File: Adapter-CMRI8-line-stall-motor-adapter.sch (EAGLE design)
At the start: 4 parts

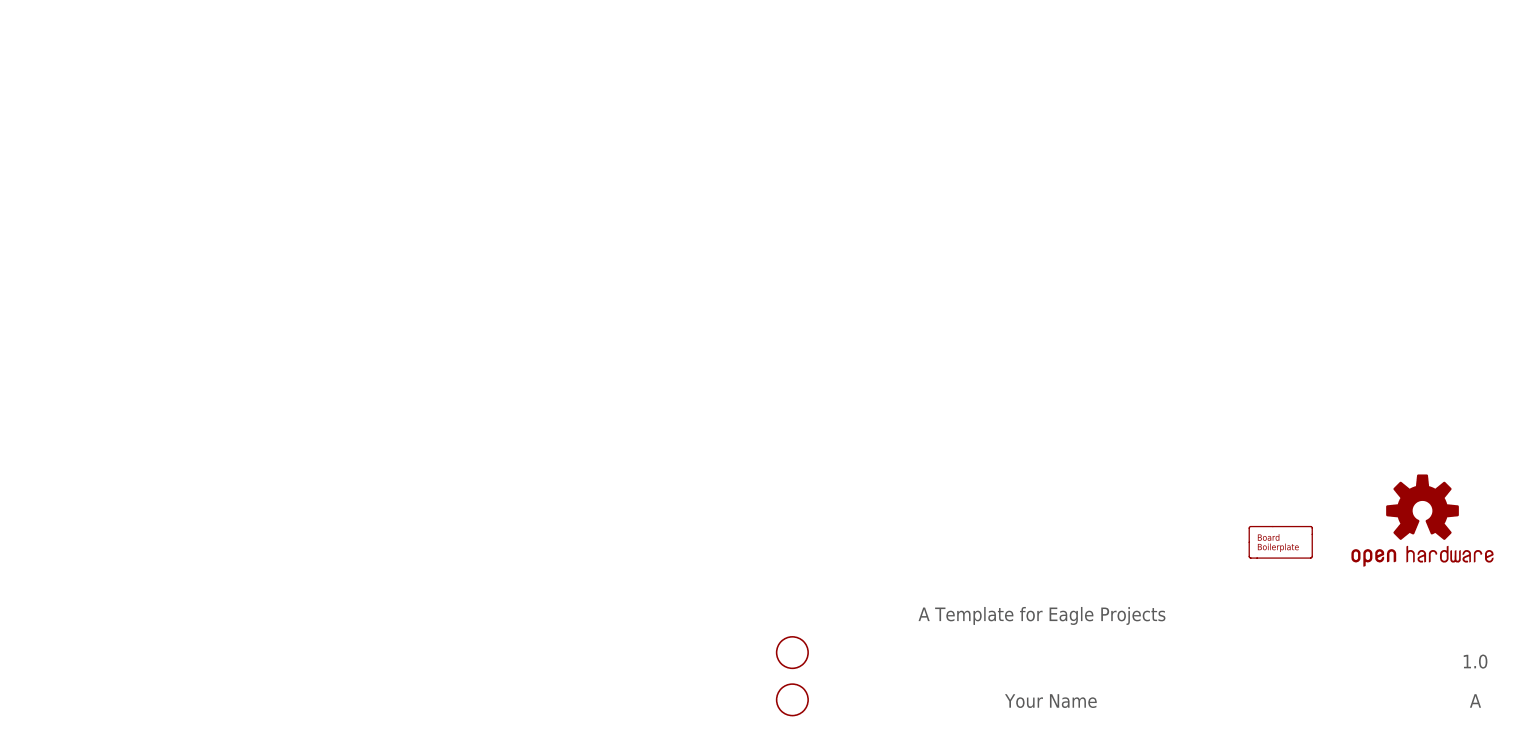
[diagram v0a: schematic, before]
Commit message: added the CMRI-35mm board as a start
modifying the CMRI-3.5 mm board
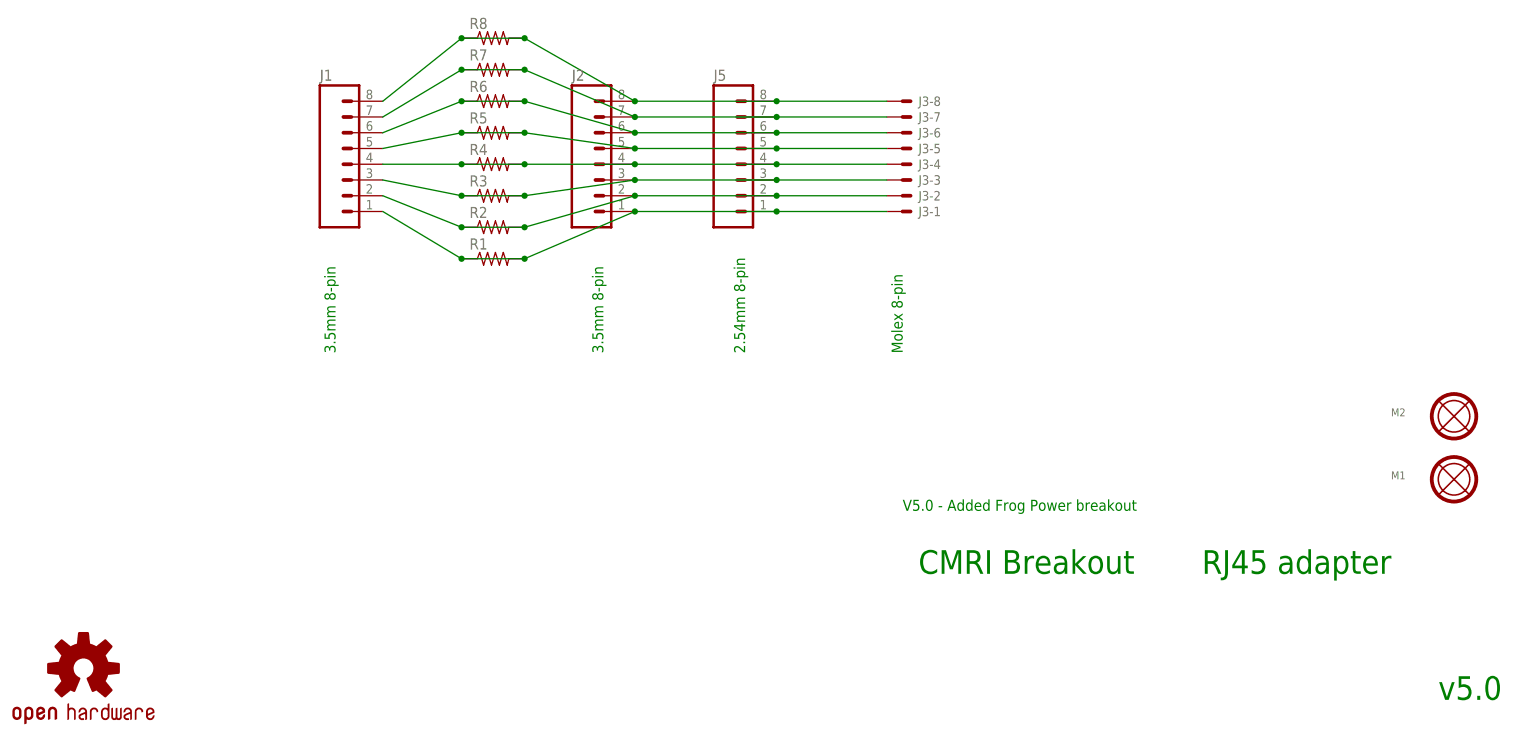
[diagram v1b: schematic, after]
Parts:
- removed BOARD1: BOARD80X100, SPCoast:BOARD80X100
- removed FID1, FID2: FIDUCIAL, SPCoast:FIDUCIAL
- removed OSHW1: DOC-OSHW-LOGO-M, SPCoast:DOC-OSHW-LOGO-M
- added J1, J2: (no value), SPCoast:CONNECTOR-M083.5MM-8
- added J3: (no value), SPCoast:KK-156-8F
- added J5: (no value), SPCoast:CONNECTOR-M08LOCK
- added M1, M2: MOUNTINGHOLE, SPCoast:MOUNTINGHOLE
- added R1, R2, R3, R4, R5, R6, R7, R8: (no value), SPCoast:RPTH04
- added U$1: DOC-OSHW-LOGO-L, SPCoast:DOC-OSHW-LOGO-L
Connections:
- new net L1: J1.1, J2.1, J3-1.S, J5.1, R1.1, R1.2
- new net L2: J1.2, J2.2, J3-2.S, J5.2, R2.1, R2.2
- new net L3: J1.3, J2.3, J3-3.S, J5.3, R3.1, R3.2
- new net L4: J1.4, J2.4, J3-4.S, J5.4, R4.1, R4.2
- new net L5: J1.5, J2.5, J3-5.S, J5.5, R5.1, R5.2
- new net L6: J1.6, J2.6, J3-6.S, J5.6, R6.1, R6.2
- new net L7: J1.7, J2.7, J3-7.S, J5.7, R7.1, R7.2
- new net L8: J1.8, J2.8, J3-8.S, J5.8, R8.1, R8.2
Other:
- note added: "2.54mm 8-pin"
- note added: "3.5mm 8-pin"
- note added: "CMRI Breakout"
- note added: "Molex 8-pin"
- note added: "RJ45 adapter"
- note added: "V5.0 - Added Frog Power breakout"
- note added: "v5.0"
- note removed: "1.0"
- note removed: "A"
- note removed: "A Template for Eagle Projects"
- note removed: "Your Name"
